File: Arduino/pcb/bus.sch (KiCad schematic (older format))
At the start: 4 parts, among them J2 Floppy-Bus, J3 MAX485 Socket, J4 Floppy-Bus

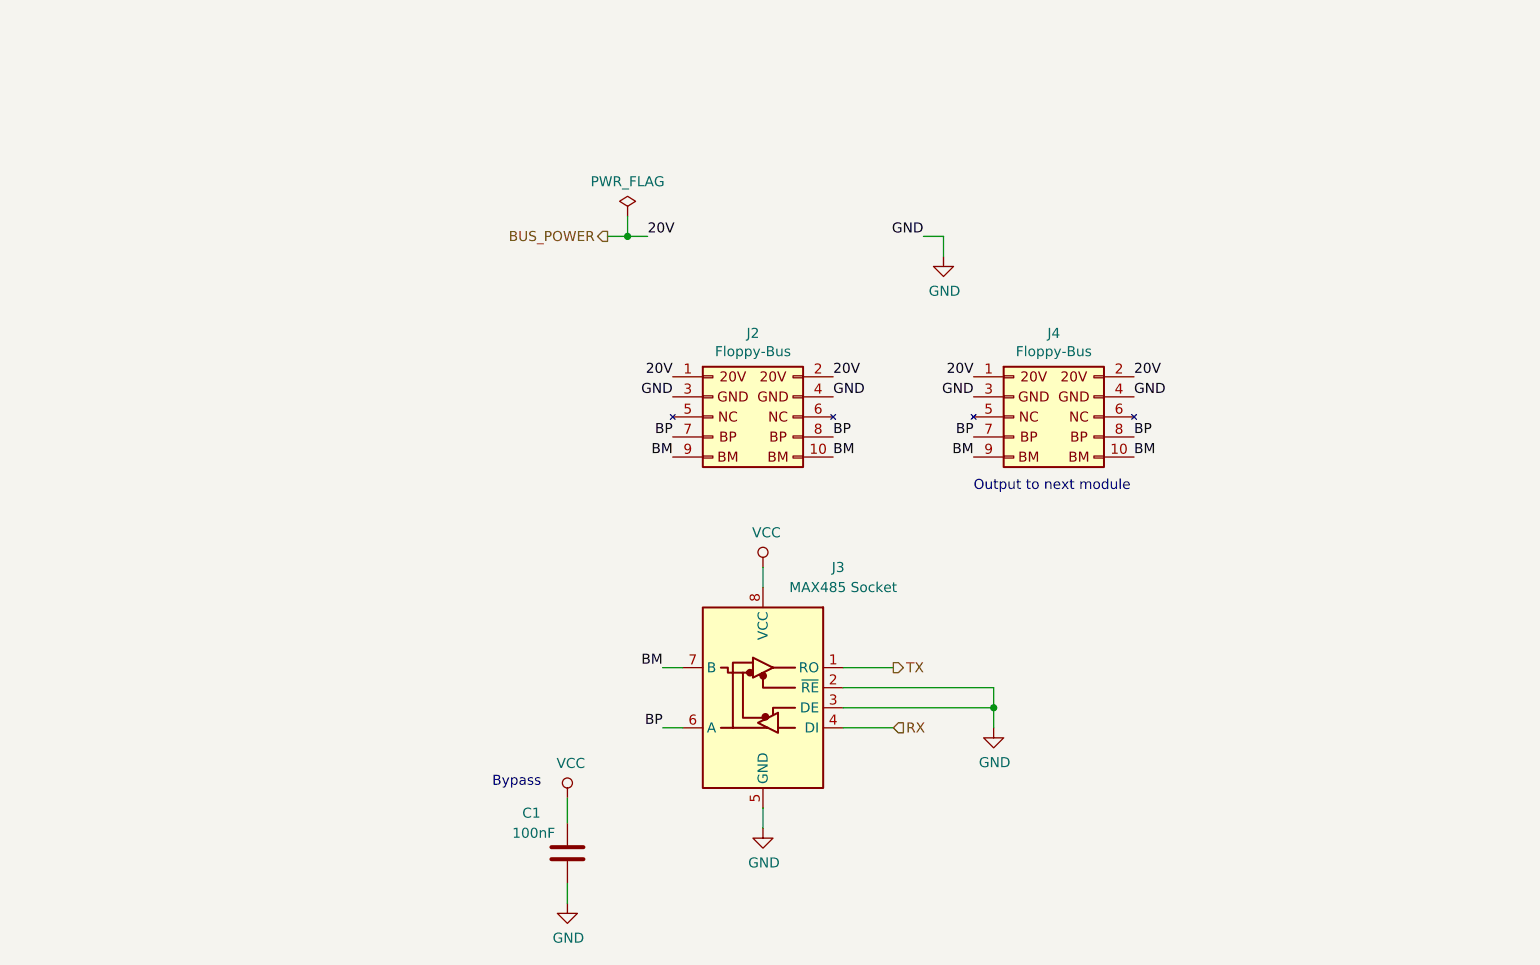
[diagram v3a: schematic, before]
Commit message: pcb: bus: more descriptive text for bus connectors
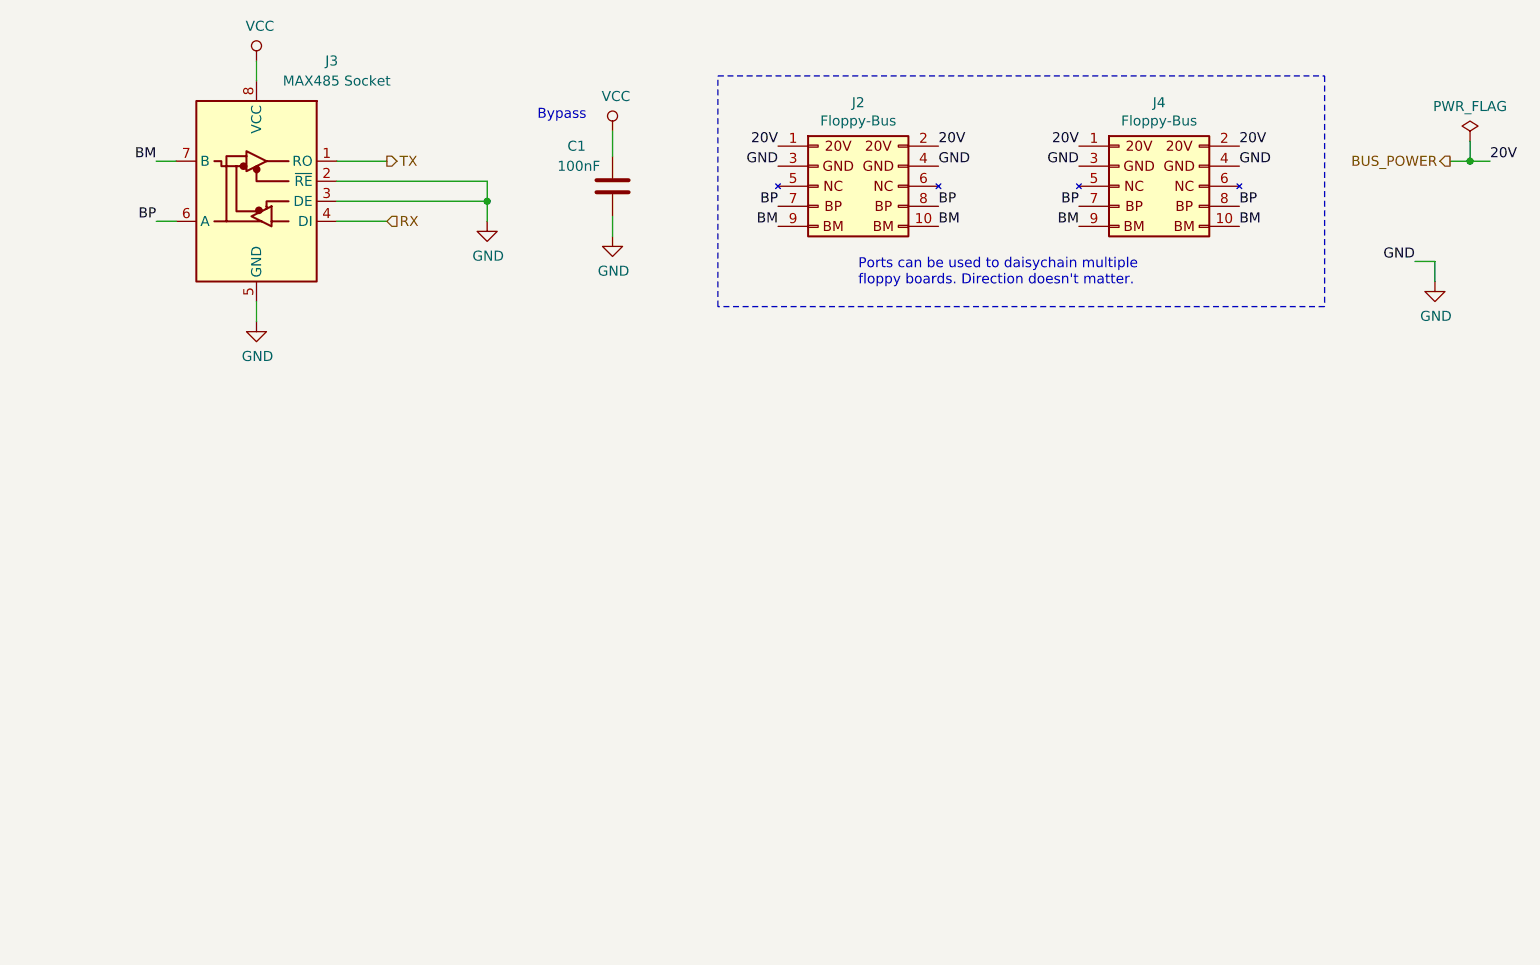
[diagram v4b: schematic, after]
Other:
- note added: "Ports can be used to daisychain multiple\nfloppy boards. Direction doesn't matter."
- note removed: "Output to next module"
- moved on the sheet: C1, J2, J3, J4
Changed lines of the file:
@@
 L Interface_UART:MAX485E J3
 U 1 1 5CF1EB96
-P 7275 3925
-F 0 "J3" H 6900 4525 50  0000 C CNN
-F 1 "MAX485 Socket" H 6875 4425 50  0000 C CNN
-F 2 "dil:dil_8-300_socket" H 7275 3925 50  0001 C CNN
-F 3 "" H 7275 3925 50  0001 C CNN
-	1    7275 3925
+P 4750 1400
+F 0 "J3" H 4375 2000 50  0000 C CNN
+F 1 "MAX485 Socket" H 4350 1900 50  0000 C CNN
+F 2 "dil:dil_8-300_socket" H 4750 1400 50  0001 C CNN
+F 3 "" H 4750 1400 50  0001 C CNN
+	1    4750 1400
 	-1   0    0    -1
 $EndComp
-Text Notes 8325 2950 0    50   ~ 0
-Output to next module
 $Comp
 L power:VCC #PWR04
 U 1 1 5CF1EBBB
-P 7275 3325
-F 0 "#PWR04" H 7275 3175 50  0001 C CNN
-F 1 "VCC" H 7292 3498 50  0000 C CNN
-F 2 "" H 7275 3325 50  0001 C CNN
-F 3 "" H 7275 3325 50  0001 C CNN
-	1    7275 3325
+P 4750 800
+F 0 "#PWR04" H 4750 650 50  0001 C CNN
+F 1 "VCC" H 4767 973 50  0000 C CNN
+F 2 "" H 4750 800 50  0001 C CNN
+F 3 "" H 4750 800 50  0001 C CNN
+	1    4750 800
 	1    0    0    -1
 $EndComp
@@
 L power:GND #PWR05
 U 1 1 5CF1EBC1
-P 7275 4625
-F 0 "#PWR05" H 7275 4375 50  0001 C CNN
-F 1 "GND" H 7280 4452 50  0000 C CNN
-F 2 "" H 7275 4625 50  0001 C CNN
-F 3 "" H 7275 4625 50  0001 C CNN
-	1    7275 4625
-	1    0    0    -1
-$EndComp
-Wire Wire Line
-	7275 3425 7275 3325
-Wire Wire Line
-	7275 4525 7275 4625
-Wire Wire Line
-	7675 3825 7925 3825
-Wire Wire Line
-	7675 4125 7925 4125
-Wire Wire Line
-	7675 4025 8425 4025
-Wire Wire Line
-	7675 3925 8425 3925
-Wire Wire Line
-	8425 3925 8425 4025
-Connection ~ 8425 4025
+P 4750 2100
+F 0 "#PWR05" H 4750 1850 50  0001 C CNN
+F 1 "GND" H 4755 1927 50  0000 C CNN
+F 2 "" H 4750 2100 50  0001 C CNN
+F 3 "" H 4750 2100 50  0001 C CNN
+	1    4750 2100
+	1    0    0    -1
+$EndComp
+Wire Wire Line
+	4750 900  4750 800
+Wire Wire Line
+	4750 2000 4750 2100
+Wire Wire Line
+	5150 1300 5400 1300
+Wire Wire Line
+	5150 1600 5400 1600
+Wire Wire Line
+	5150 1500 5900 1500
+Wire Wire Line
+	5150 1400 5900 1400
+Wire Wire Line
+	5900 1400 5900 1500
+Connection ~ 5900 1500
 $Comp
 L power:GND #PWR07
 U 1 1 5CF1EBD6
-P 8425 4125
-F 0 "#PWR07" H 8425 3875 50  0001 C CNN
-F 1 "GND" H 8430 3952 50  0000 C CNN
-F 2 "" H 8425 4125 50  0001 C CNN
-F 3 "" H 8425 4125 50  0001 C CNN
-	1    8425 4125
-	1    0    0    -1
-$EndComp
-Wire Wire Line
-	8425 4025 8425 4125
-Text HLabel 7925 3825 2    50   Output ~ 0
+P 5900 1600
+F 0 "#PWR07" H 5900 1350 50  0001 C CNN
+F 1 "GND" H 5905 1427 50  0000 C CNN
+F 2 "" H 5900 1600 50  0001 C CNN
+F 3 "" H 5900 1600 50  0001 C CNN
+	1    5900 1600
+	1    0    0    -1
+$EndComp
+Wire Wire Line
+	5900 1500 5900 1600
+Text HLabel 5400 1300 2    50   Output ~ 0
 TX
-Text HLabel 7925 4125 2    50   Input ~ 0
+Text HLabel 5400 1600 2    50   Input ~ 0
 RX
-Text HLabel 6500 1675 0    50   Output ~ 0
+Text HLabel 10700 1300 0    50   Output ~ 0
 BUS_POWER
 $Comp
 L Device:C C?
 U 1 1 5D17F33C
-P 6300 4750
+P 6525 1425
 AR Path="/5D17F33C" Ref="C?"  Part="1"
 AR Path="/5CCFEC3E/5D17F33C" Ref="C?"  Part="1"
 AR Path="/5CD1E0A5/5D17F33C" Ref="C1"  Part="1"
-F 0 "C1" H 6075 4950 50  0000 L CNN
-F 1 "100nF" H 6025 4850 50  0000 L CNN
-F 2 "Capacitor_SMD:C_0805_2012Metric" H 6338 4600 50  0001 C CNN
-F 3 "~" H 6300 4750 50  0001 C CNN
-	1    6300 4750
+F 0 "C1" H 6300 1625 50  0000 L CNN
+F 1 "100nF" H 6250 1525 50  0000 L CNN
+F 2 "Capacitor_SMD:C_0805_2012Metric" H 6563 1275 50  0001 C CNN
+F 3 "~" H 6525 1425 50  0001 C CNN
+	1    6525 1425
 	1    0    0    -1
 $EndComp
@@
 L power:VCC #PWR?
 U 1 1 5D17F342
-P 6300 4475
+P 6525 1150
 AR Path="/5CCFEC3E/5D17F342" Ref="#PWR?"  Part="1"
 AR Path="/5CD1E0A5/5D17F342" Ref="#PWR02"  Part="1"
-F 0 "#PWR02" H 6300 4325 50  0001 C CNN
-F 1 "VCC" H 6317 4648 50  0000 C CNN
-F 2 "" H 6300 4475 50  0001 C CNN
-F 3 "" H 6300 4475 50  0001 C CNN
-	1    6300 4475
+F 0 "#PWR02" H 6525 1000 50  0001 C CNN
+F 1 "VCC" H 6542 1323 50  0000 C CNN
+F 2 "" H 6525 1150 50  0001 C CNN
+F 3 "" H 6525 1150 50  0001 C CNN
+	1    6525 1150
 	1    0    0    -1
 $EndComp
@@
 L power:GND #PWR?
 U 1 1 5D17F348
-P 6300 5000
+P 6525 1675
 AR Path="/5CCFEC3E/5D17F348" Ref="#PWR?"  Part="1"
 AR Path="/5CD1E0A5/5D17F348" Ref="#PWR03"  Part="1"
-F 0 "#PWR03" H 6300 4750 50  0001 C CNN
-F 1 "GND" H 6305 4827 50  0000 C CNN
-F 2 "" H 6300 5000 50  0001 C CNN
-F 3 "" H 6300 5000 50  0001 C CNN
-	1    6300 5000
-	1    0    0    -1
-$EndComp
-Wire Wire Line
-	6300 4475 6300 4600
-Wire Wire Line
-	6300 4900 6300 5000
-Text Notes 5925 4425 0    50   ~ 0
+F 0 "#PWR03" H 6525 1425 50  0001 C CNN
+F 1 "GND" H 6530 1502 50  0000 C CNN
+F 2 "" H 6525 1675 50  0001 C CNN
+F 3 "" H 6525 1675 50  0001 C CNN
+	1    6525 1675
+	1    0    0    -1
+$EndComp
+Wire Wire Line
+	6525 1150 6525 1275
+Wire Wire Line
+	6525 1575 6525 1675
+Text Notes 6150 1100 0    50   ~ 0
 Bypass
 $Comp
 L power:PWR_FLAG #FLG01
 U 1 1 5D1B34B5
-P 6600 1575
-F 0 "#FLG01" H 6600 1650 50  0001 C CNN
-F 1 "PWR_FLAG" H 6600 1748 50  0000 C CNN
-F 2 "" H 6600 1575 50  0001 C CNN
-F 3 "~" H 6600 1575 50  0001 C CNN
-	1    6600 1575
-	1    0    0    -1
-$EndComp
-Text Label 6700 1675 0    50   ~ 0
-20V
-Text Label 6775 4125 2    50   ~ 0
-BP
-Text Label 6775 3825 2    50   ~ 0
-BM
-Wire Wire Line
-	6700 1675 6600 1675
-Wire Wire Line
-	6500 1675 6600 1675
-Connection ~ 6600 1675
+P 10800 1200
+F 0 "#FLG01" H 10800 1275 50  0001 C CNN
+F 1 "PWR_FLAG" H 10800 1373 50  0000 C CNN
+F 2 "" H 10800 1200 50  0001 C CNN
+F 3 "~" H 10800 1200 50  0001 C CNN
+	1    10800 1200
+	1    0    0    -1
+$EndComp
+Text Label 10900 1300 0    50   ~ 0
+20V
+Text Label 4250 1600 2    50   ~ 0
+BP
+Text Label 4250 1300 2    50   ~ 0
+BM
+Wire Wire Line
+	10900 1300 10800 1300
+Wire Wire Line
+	10700 1300 10800 1300
+Connection ~ 10800 1300
 $Comp
 L floppy-bus-connector:Floppy-Bus J4
 U 1 1 5D1ABE61
-P 8525 2575
-F 0 "J4" H 8725 2992 50  0000 C CNN
-F 1 "Floppy-Bus" H 8725 2901 50  0000 C CNN
-F 2 "shrouded:Shrouded_Header_2x05_Pitch2.54mm" H 8525 2575 50  0001 C CNN
-F 3 "" H 8525 2575 50  0001 C CNN
-	1    8525 2575
-	1    0    0    -1
-$EndComp
-Wire Wire Line
-	6600 1575 6600 1675
-Wire Wire Line
-	6875 3825 6775 3825
-Wire Wire Line
-	6875 4125 6775 4125
-Text Label 6825 2375 2    50   ~ 0
-20V
-Text Label 7625 2375 0    50   ~ 0
-20V
-Text Label 8325 2375 2    50   ~ 0
-20V
-Text Label 9125 2375 0    50   ~ 0
+P 9050 1425
+F 0 "J4" H 9250 1842 50  0000 C CNN
+F 1 "Floppy-Bus" H 9250 1751 50  0000 C CNN
+F 2 "shrouded:Shrouded_Header_2x05_Pitch2.54mm" H 9050 1425 50  0001 C CNN
+F 3 "" H 9050 1425 50  0001 C CNN
+	1    9050 1425
+	1    0    0    -1
+$EndComp
+Wire Wire Line
+	10800 1200 10800 1300
+Wire Wire Line
+	4350 1300 4250 1300
+Wire Wire Line
+	4350 1600 4250 1600
+Text Label 7350 1225 2    50   ~ 0
+20V
+Text Label 8150 1225 0    50   ~ 0
+20V
+Text Label 8850 1225 2    50   ~ 0
+20V
+Text Label 9650 1225 0    50   ~ 0
 20V
 $Comp
 L power:GND #PWR06
 U 1 1 5CDB5675
-P 8175 1775
-F 0 "#PWR06" H 8175 1525 50  0001 C CNN
-F 1 "GND" H 8180 1602 50  0000 C CNN
-F 2 "" H 8175 1775 50  0001 C CNN
-F 3 "" H 8175 1775 50  0001 C CNN
-	1    8175 1775
-	1    0    0    -1
-$EndComp
-Text Label 8075 1675 2    50   ~ 0
-GND
-Wire Wire Line
-	8075 1675 8175 1675
-Wire Wire Line
-	8175 1675 8175 1775
-Text Label 7625 2475 0    50   ~ 0
-GND
-Text Label 8325 2475 2    50   ~ 0
-GND
-Text Label 9125 2475 0    50   ~ 0
-GND
-Text Label 6825 2475 2    50   ~ 0
+P 10625 1900
+F 0 "#PWR06" H 10625 1650 50  0001 C CNN
+F 1 "GND" H 10630 1727 50  0000 C CNN
+F 2 "" H 10625 1900 50  0001 C CNN
+F 3 "" H 10625 1900 50  0001 C CNN
+	1    10625 1900
+	1    0    0    -1
+$EndComp
+Text Label 10525 1800 2    50   ~ 0
+GND
+Wire Wire Line
+	10525 1800 10625 1800
+Wire Wire Line
+	10625 1800 10625 1900
+Text Label 8150 1325 0    50   ~ 0
+GND
+Text Label 8850 1325 2    50   ~ 0
+GND
+Text Label 9650 1325 0    50   ~ 0
+GND
+Text Label 7350 1325 2    50   ~ 0
 GND
 $Comp
 L floppy-bus-connector:Floppy-Bus J2
 U 1 1 5D1AADEF
-P 7025 2575
-F 0 "J2" H 7225 2992 50  0000 C CNN
-F 1 "Floppy-Bus" H 7225 2901 50  0000 C CNN
-F 2 "shrouded:Shrouded_Header_2x05_Pitch2.54mm" H 7025 2575 50  0001 C CNN
-F 3 "" H 7025 2575 50  0001 C CNN
-	1    7025 2575
-	1    0    0    -1
-$EndComp
-Text Label 6825 2675 2    50   ~ 0
-BP
-Text Label 6825 2775 2    50   ~ 0
-BM
-Text Label 7625 2675 0    50   ~ 0
-BP
-Text Label 9125 2675 0    50   ~ 0
-BP
-Text Label 8325 2675 2    50   ~ 0
-BP
-Text Label 8325 2775 2    50   ~ 0
-BM
-Text Label 7625 2775 0    50   ~ 0
-BM
-Text Label 9125 2775 0    50   ~ 0
-BM
+P 7550 1425
+F 0 "J2" H 7750 1842 50  0000 C CNN
+F 1 "Floppy-Bus" H 7750 1751 50  0000 C CNN
+F 2 "shrouded:Shrouded_Header_2x05_Pitch2.54mm" H 7550 1425 50  0001 C CNN
+F 3 "" H 7550 1425 50  0001 C CNN
+	1    7550 1425
+	1    0    0    -1
+$EndComp
+Text Label 7350 1525 2    50   ~ 0
+BP
+Text Label 7350 1625 2    50   ~ 0
+BM
+Text Label 8150 1525 0    50   ~ 0
+BP
+Text Label 9650 1525 0    50   ~ 0
+BP
+Text Label 8850 1525 2    50   ~ 0
+BP
+Text Label 8850 1625 2    50   ~ 0
+BM
+Text Label 8150 1625 0    50   ~ 0
+BM
+Text Label 9650 1625 0    50   ~ 0
+BM
+Text Notes 7750 1925 0    50   ~ 0
+Ports can be used to daisychain multiple\nfloppy boards. Direction doesn't matter.
+Wire Notes Line
+	10075 2025 7050 2025
+Wire Notes Line
+	7050 2025 7050 875
+Wire Notes Line
+	7050 875  10075 875
+Wire Notes Line
+	10075 875  10075 2025
 $EndSCHEMATC

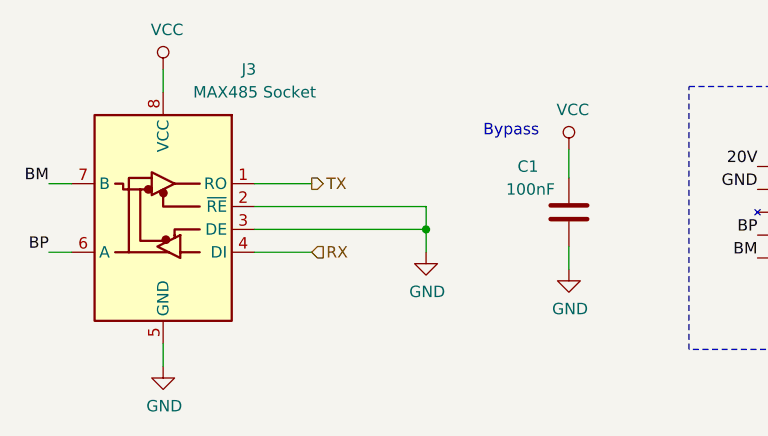
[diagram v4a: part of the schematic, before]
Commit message: pcb: mcu / bus: improve TX/RX labels for RS485 transceiver
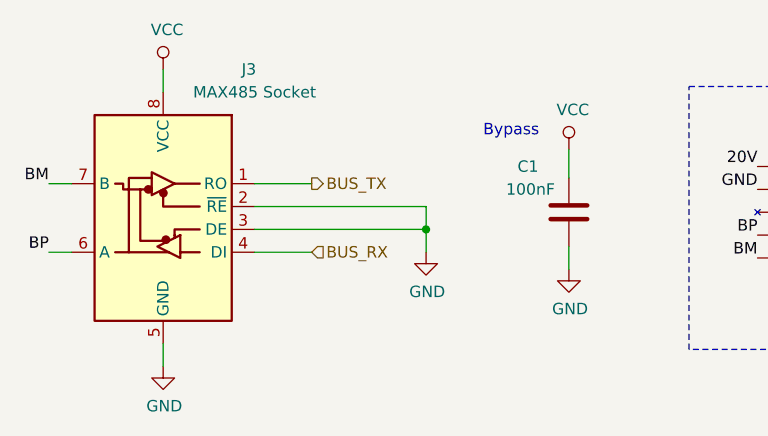
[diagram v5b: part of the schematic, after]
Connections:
- net RX renamed BUS_RX
- net TX renamed BUS_TX
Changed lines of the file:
@@
 	5900 1500 5900 1600
 Text HLabel 5400 1300 2    50   Output ~ 0
-TX
+BUS_TX
 Text HLabel 5400 1600 2    50   Input ~ 0
-RX
+BUS_RX
 Text HLabel 10700 1300 0    50   Output ~ 0
 BUS_POWER
